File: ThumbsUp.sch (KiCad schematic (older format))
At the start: 153 parts, among them IC1 RP2040, IC2 W25Q128JVSIM, IC3 RP2040, IC4 W25Q128JVSIM, J1 Conn_01x04_Male, J10 Raiser_Male, J11 Raiser_Female, J12 Raiser_Male, J13 Raiser_Female, J14 Raiser_Male, J15 Raiser_Female, J16 Raiser_Male, J17 Raiser_Female, J18 Raiser_Male, J19 Raiser_Female, J2 Conn_01x04_Male, J20 Conn_01x04_Female, J21 Conn_01x04_Female, J22 Conn_01x04_Female, J23 Conn_01x04_Female, J24 Conn_01x04_Male, J25 Conn_01x04_Male, J26 Conn_01x04_Male, J27 Conn_01x04_Male, J28 Conn_01x04_Female, J29 Conn_01x04_Female, J3 Conn_01x04_Female, J30 Conn_01x04_Female, J31 Conn_01x04_Female, J32 USB_C_Receptacle_USB2.0, J33 Raiser_Male, J34 Raiser_Female, J35 Raiser_Male, J36 STX-3501-3N, J37 USB_C_Receptacle_USB2.0, J38 Raiser_Female, J39 Raiser_Male, J4 Conn_01x04_Male, J40 Raiser_Female, J41 Raiser_Male, J42 Raiser_Female, J43 Raiser_Male, J44 Raiser_Female, J45 Raiser_Male, J46 STX-3501-3N, J47 Raiser_Female, J48 Raiser_Male, J5 Conn_01x04_Female, J6 Conn_01x04_Male, J7 Conn_01x04_Male, J8 Conn_01x04_Male, J9 Raiser_Female, U1 NCP1117-3.3_SOT223, U2 NCP1117-3.3_SOT223, Y1 ABLS-12.000MHZ-B4-T, Y2 ABLS-12.000MHZ-B4-T

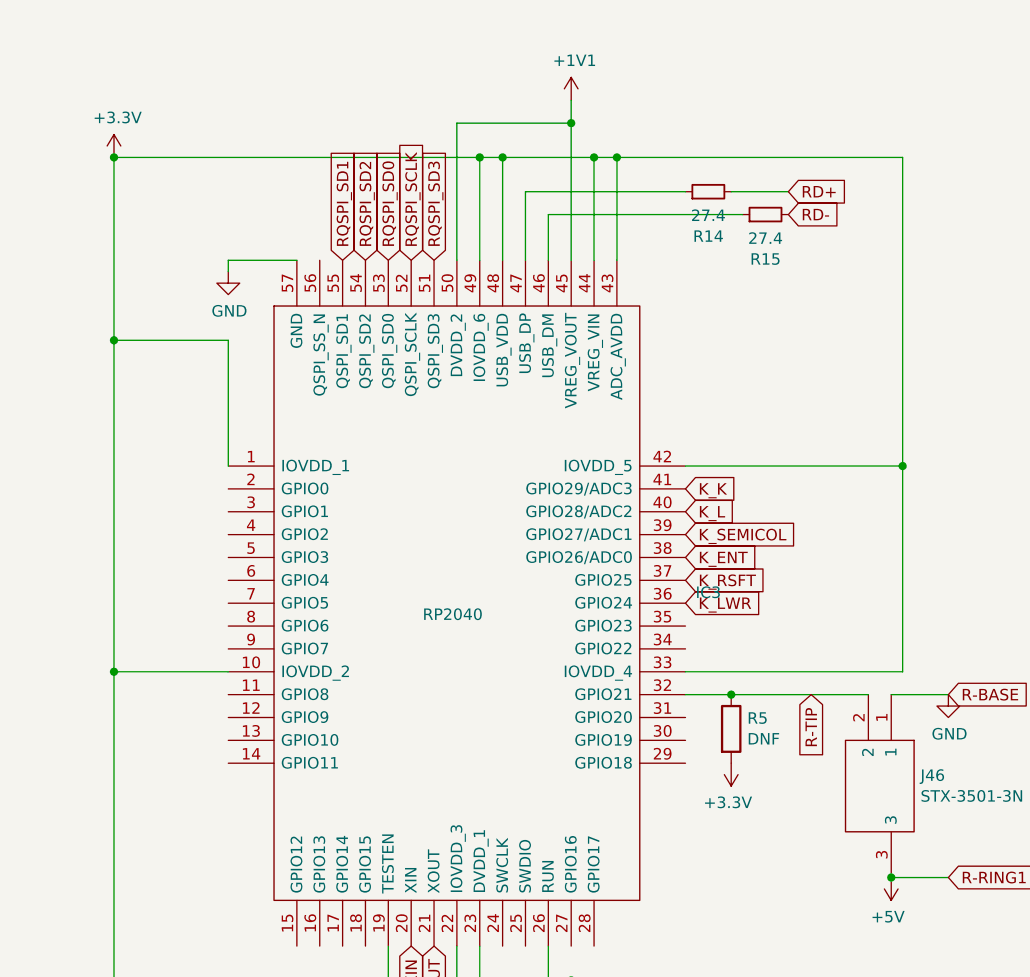
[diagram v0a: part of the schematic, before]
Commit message: Tracing the plates.
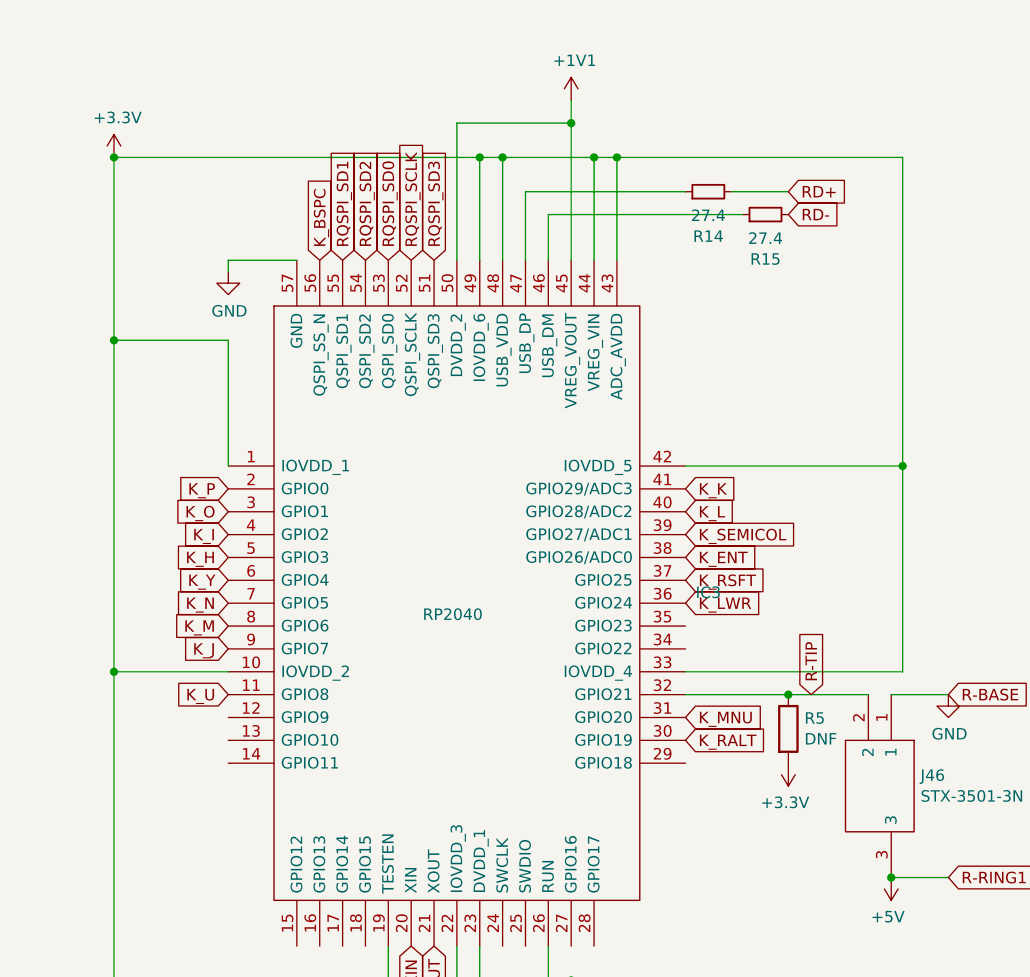
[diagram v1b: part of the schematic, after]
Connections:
- net K_BSPC: now also IC3.56 (QSPI_SS_N)
- net K_H: now also IC3.5 (GPIO3)
- net K_I: now also IC3.4 (GPIO2)
- net K_J: now also IC3.9 (GPIO7)
- net K_M: now also IC3.8 (GPIO6)
- net K_MNU: now also IC3.31 (GPIO20)
- net K_N: now also IC3.7 (GPIO5)
- net K_O: now also IC3.3 (GPIO1)
- net K_P: now also IC3.2 (GPIO0)
- net K_RALT: now also IC3.30 (GPIO19)
- net K_U: now also IC3.11 (GPIO8)
- net K_Y: now also IC3.6 (GPIO4)
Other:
- moved on the sheet: R5
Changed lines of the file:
@@
 $EndComp
 Connection ~ 11950 4600
-Wire Wire Line
-	12050 9600 12050 7950
-$Comp
-L RP2040:RP2040 IC3
-U 1 1 63C3395F
-P 12550 7050
-F 0 "IC3" H 14594 6496 50  0000 L CNN
-F 1 "RP2040" H 13400 6400 50  0000 L CNN
-F 2 "RP2040:QFN40P700X700X90-57N-D" H 14400 7750 50  0001 L CNN
-F 3 "https://datasheets.raspberrypi.org/rp2040/rp2040-datasheet.pdf" H 14400 7650 50  0001 L CNN
-F 4 "Microcontroller in QFN Package" H 14400 7550 50  0001 L CNN "Description"
-F 5 "0.9" H 14400 7450 50  0001 L CNN "Height"
-F 6 "RASPBERRY-PI" H 14400 7350 50  0001 L CNN "Manufacturer_Name"
-F 7 "RP2040" H 14400 7250 50  0001 L CNN "Manufacturer_Part_Number"
-F 8 "" H 14400 7150 50  0001 L CNN "Mouser Part Number"
-F 9 "" H 14400 7050 50  0001 L CNN "Mouser Price/Stock"
-F 10 "" H 14400 6950 50  0001 L CNN "Arrow Part Number"
-F 11 "" H 14400 6850 50  0001 L CNN "Arrow Price/Stock"
-F 12 "" H 14400 6750 50  0001 L CNN "Mouser Testing Part Number"
-F 13 "" H 14400 6650 50  0001 L CNN "Mouser Testing Price/Stock"
-	1    12550 7050
-	1    0    0    -1
-$EndComp
 $Comp
 L Device:R_Small R11
@@
 Connection ~ 12050 6500
 Wire Wire Line
-	12050 6500 12050 7950
-Wire Wire Line
 	1750 5750 1750 6600
 Wire Wire Line
@@
 Wire Wire Line
 	15450 8850 15700 8850
-Text GLabel 15100 8050 3    50   Input ~ 0
+Text GLabel 15100 8050 1    50   Input ~ 0
 R-TIP
 Text GLabel 15700 8050 2    50   Input ~ 0
@@
 L Device:R R5
 U 1 1 63C447F1
-P 14750 8200
-F 0 "R5" H 14820 8246 50  0000 L CNN
-F 1 "DNF" H 14820 8155 50  0000 L CNN
-F 2 "Resistor_SMD:R_0805_2012Metric" V 14680 8200 50  0001 C CNN
-F 3 "~" H 14750 8200 50  0001 C CNN
-	1    14750 8200
+P 15000 8200
+F 0 "R5" H 15070 8246 50  0000 L CNN
+F 1 "DNF" H 15070 8155 50  0000 L CNN
+F 2 "Resistor_SMD:R_0805_2012Metric" V 14930 8200 50  0001 C CNN
+F 3 "~" H 15000 8200 50  0001 C CNN
+	1    15000 8200
 	1    0    0    -1
 $EndComp
@@
 L power:+3.3V #PWR0151
 U 1 1 63C447F7
-P 14750 8350
-F 0 "#PWR0151" H 14750 8200 50  0001 C CNN
-F 1 "+3.3V" H 14765 8523 50  0000 C CNN
-F 2 "" H 14750 8350 50  0001 C CNN
-F 3 "" H 14750 8350 50  0001 C CNN
-	1    14750 8350
-	-1   0    0    1
-$EndComp
-Wire Wire Line
-	14550 8050 14750 8050
-Connection ~ 14750 8050
-Wire Wire Line
-	14750 8050 15350 8050
+P 15000 8350
+F 0 "#PWR0151" H 15000 8200 50  0001 C CNN
+F 1 "+3.3V" H 15015 8523 50  0000 C CNN
+F 2 "" H 15000 8350 50  0001 C CNN
+F 3 "" H 15000 8350 50  0001 C CNN
+	1    15000 8350
+	-1   0    0    1
+$EndComp
 Wire Wire Line
 	18500 2450 18800 2450
@@
 Text GLabel 14550 7650 2    50   Input ~ 0
 K_LWR
+Text GLabel 14550 8150 2    50   Input ~ 0
+K_MNU
+Text GLabel 14550 8250 2    50   Input ~ 0
+K_RALT
+Wire Wire Line
+	12050 9600 12050 7950
+Wire Wire Line
+	12050 6500 12050 7950
+$Comp
+L RP2040:RP2040 IC3
+U 1 1 63C3395F
+P 12550 7050
+F 0 "IC3" H 14594 6496 50  0000 L CNN
+F 1 "RP2040" H 13400 6400 50  0000 L CNN
+F 2 "RP2040:QFN40P700X700X90-57N-D" H 14400 7750 50  0001 L CNN
+F 3 "https://datasheets.raspberrypi.org/rp2040/rp2040-datasheet.pdf" H 14400 7650 50  0001 L CNN
+F 4 "Microcontroller in QFN Package" H 14400 7550 50  0001 L CNN "Description"
+F 5 "0.9" H 14400 7450 50  0001 L CNN "Height"
+F 6 "RASPBERRY-PI" H 14400 7350 50  0001 L CNN "Manufacturer_Name"
+F 7 "RP2040" H 14400 7250 50  0001 L CNN "Manufacturer_Part_Number"
+F 8 "" H 14400 7150 50  0001 L CNN "Mouser Part Number"
+F 9 "" H 14400 7050 50  0001 L CNN "Mouser Price/Stock"
+F 10 "" H 14400 6950 50  0001 L CNN "Arrow Part Number"
+F 11 "" H 14400 6850 50  0001 L CNN "Arrow Price/Stock"
+F 12 "" H 14400 6750 50  0001 L CNN "Mouser Testing Part Number"
+F 13 "" H 14400 6650 50  0001 L CNN "Mouser Testing Price/Stock"
+	1    12550 7050
+	1    0    0    -1
+$EndComp
+Connection ~ 15000 8050
+Wire Wire Line
+	15000 8050 15350 8050
+Wire Wire Line
+	14550 8050 15000 8050
+Text GLabel 12950 6150 1    50   Input ~ 0
+K_BSPC
+Text GLabel 12550 7150 0    50   Input ~ 0
+K_P
+Text GLabel 12550 7250 0    50   Input ~ 0
+K_O
+Text GLabel 12550 7350 0    50   Input ~ 0
+K_I
+Text GLabel 12550 7450 0    50   Input ~ 0
+K_H
+Text GLabel 12550 7550 0    50   Input ~ 0
+K_Y
+Text GLabel 12550 7650 0    50   Input ~ 0
+K_N
+Text GLabel 12550 7750 0    50   Input ~ 0
+K_M
+Text GLabel 12550 7850 0    50   Input ~ 0
+K_J
+Text GLabel 12550 8050 0    50   Input ~ 0
+K_U
 $EndSCHEMATC

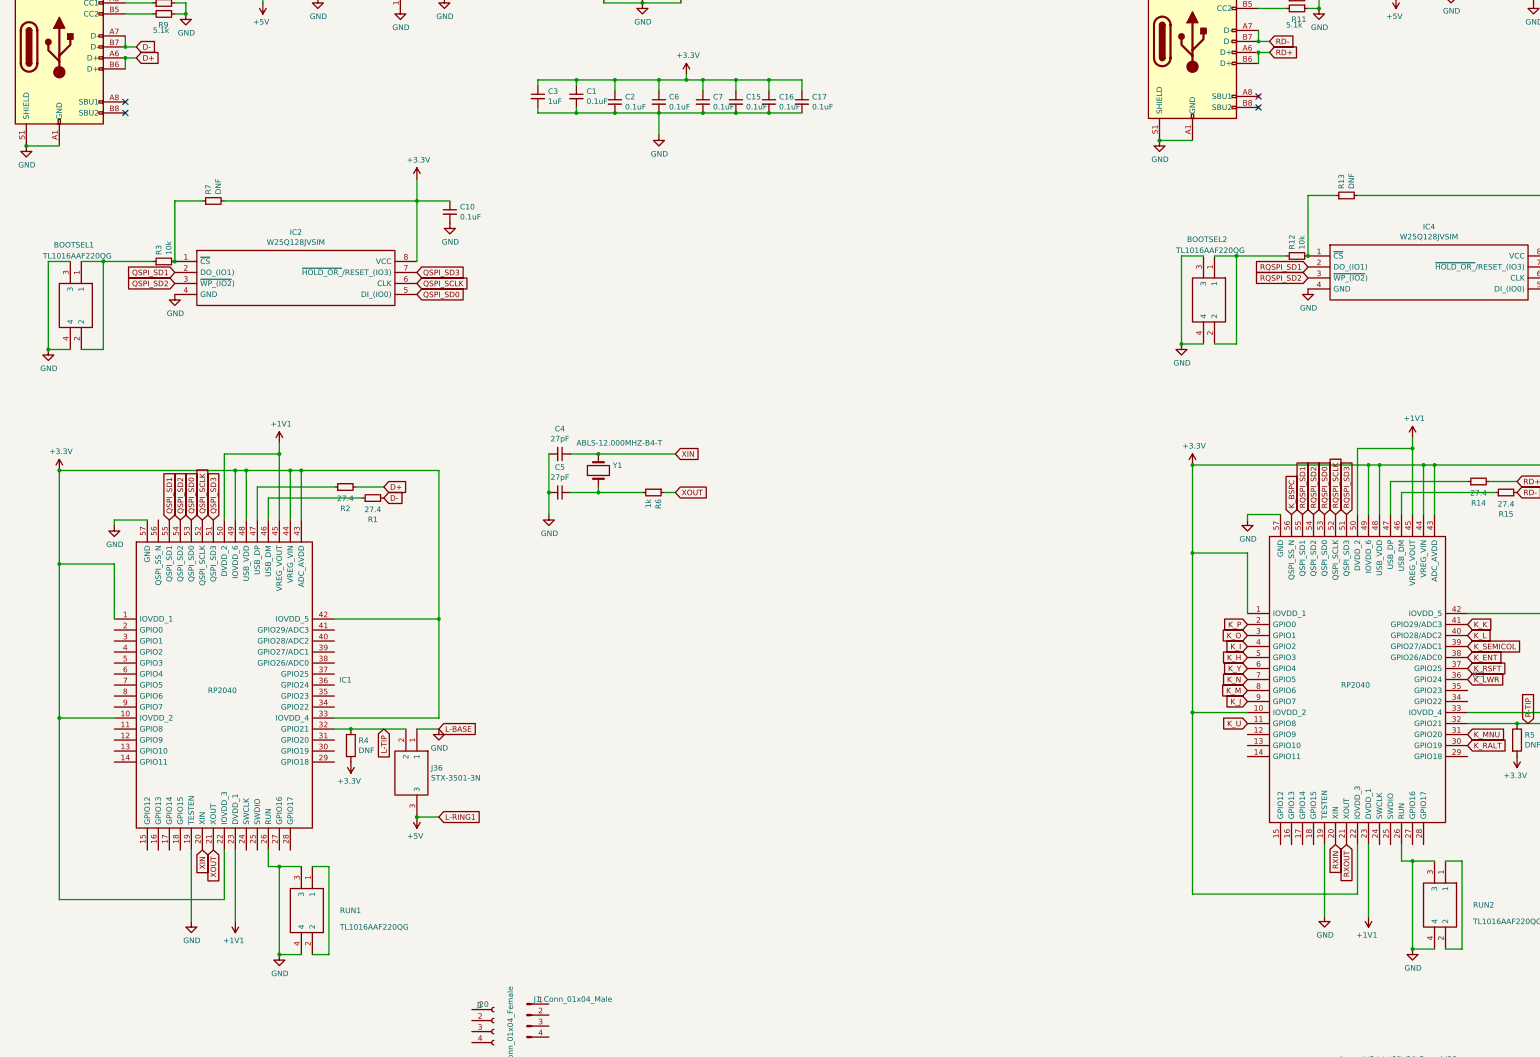
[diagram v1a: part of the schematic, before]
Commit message: Somewhat finished the PCB tracing
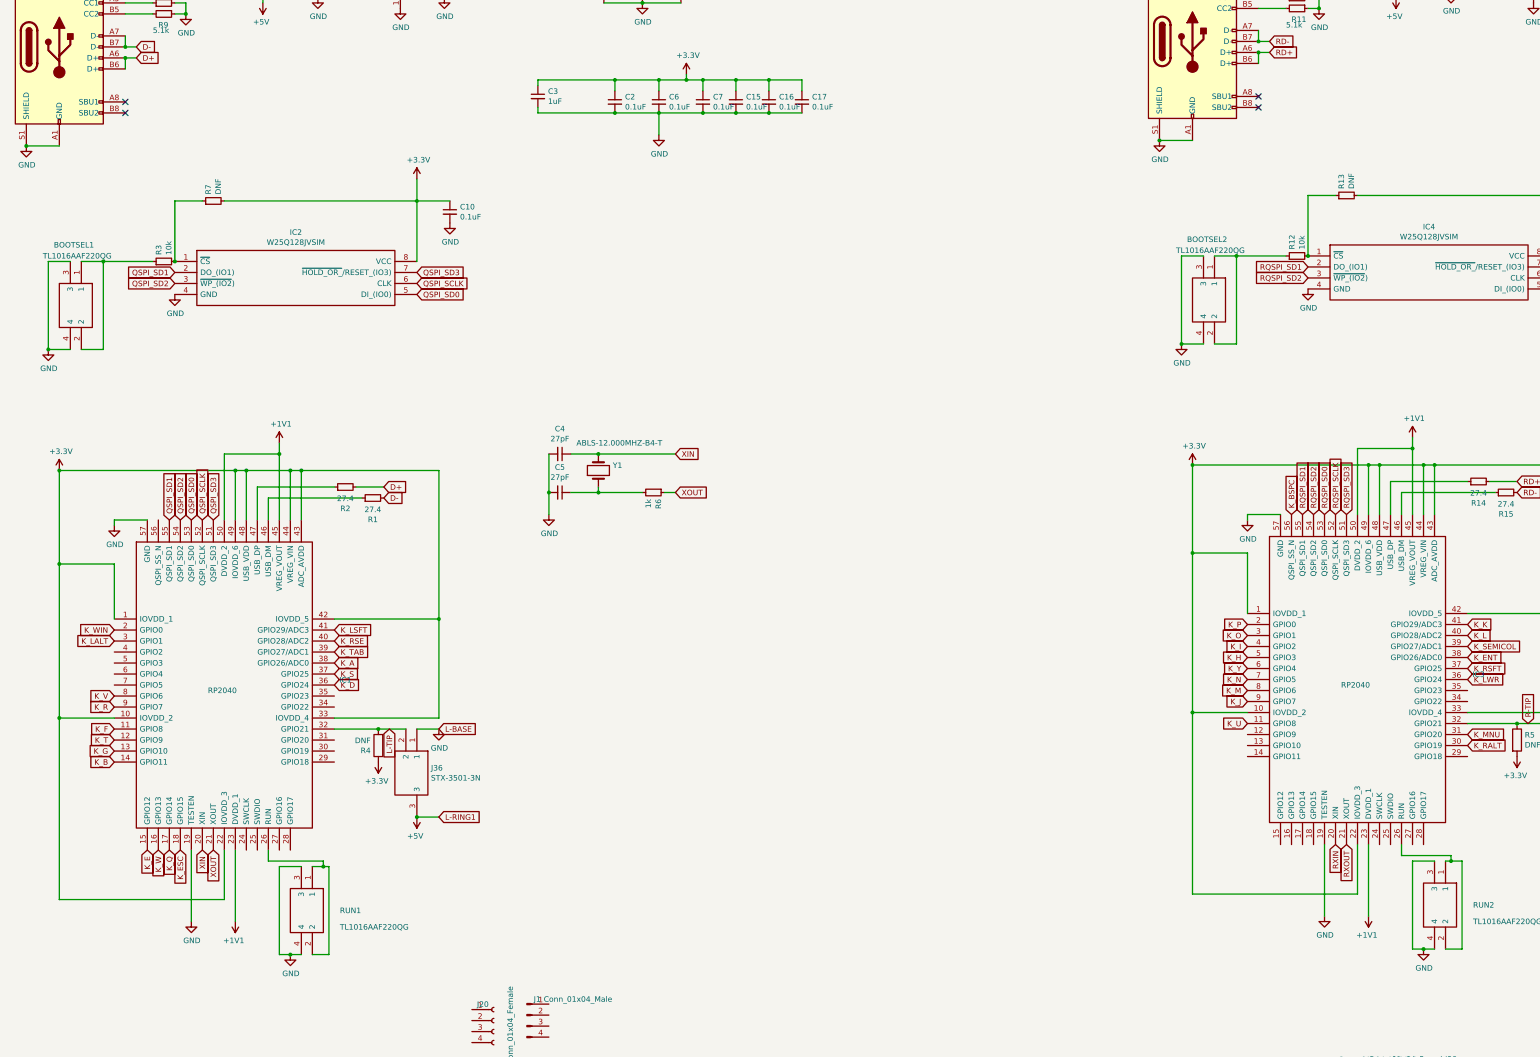
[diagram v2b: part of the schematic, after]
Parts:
- removed C1: 0.1uF, Capacitor_SMD:C_0402_1005Metric, symbol Device:C_Small
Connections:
- net +3V3: now also R4.1; no longer R4.2
- net GND: no longer IC1.26 (RUN), IC3.26 (RUN)
- net K_A: now also IC1.38 (GPIO26/ADC0)
- net K_B: now also IC1.14 (GPIO11)
- net K_D: now also IC1.36 (GPIO24)
- net K_E: now also IC1.15 (GPIO12)
- net K_ESC: now also IC1.18 (GPIO15)
- net K_F: now also IC1.11 (GPIO8)
- net K_G: now also IC1.13 (GPIO10)
- net K_LALT: now also IC1.3 (GPIO1)
- net K_LSFT: now also IC1.41 (GPIO29/ADC3)
- net K_Q: now also IC1.17 (GPIO14)
- net K_R: now also IC1.9 (GPIO7)
- net K_RSE: now also IC1.40 (GPIO28/ADC2)
- net K_S: now also IC1.37 (GPIO25)
- net K_T: now also IC1.12 (GPIO9)
- net K_TAB: now also IC1.39 (GPIO27/ADC1)
- net K_V: now also IC1.8 (GPIO6)
- net K_W: now also IC1.16 (GPIO13)
- net K_WIN: now also IC1.2 (GPIO0)
- net L-TIP: now also R4.2; no longer R4.1
- net at RUN1.1, RUN1.2: now also IC1.26 (RUN)
- net at RUN2.1, RUN2.2: now also IC3.26 (RUN)
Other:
- moved on the sheet: R4
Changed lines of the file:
@@
 Wire Wire Line
 	3300 1300 3600 1300
-$Comp
-L Device:C_Small C1
-U 1 1 6197A27B
-P 6450 2350
-F 0 "C1" H 6542 2396 50  0000 L CNN
-F 1 "0.1uF" H 6542 2305 50  0000 L CNN
-F 2 "Capacitor_SMD:C_0402_1005Metric" H 6450 2350 50  0001 C CNN
-F 3 "~" H 6450 2350 50  0001 C CNN
-	1    6450 2350
-	1    0    0    -1
-$EndComp
-Wire Wire Line
-	6800 2500 6450 2500
-Wire Wire Line
-	6450 2500 6450 2450
 Connection ~ 6800 2500
-Wire Wire Line
-	6800 2200 6450 2200
-Wire Wire Line
-	6450 2200 6450 2250
 Connection ~ 6800 2200
 Wire Wire Line
@@
 	6100 2250 6100 2200
 Wire Wire Line
-	6100 2200 6450 2200
-Connection ~ 6450 2200
-Wire Wire Line
 	6100 2450 6100 2500
-Wire Wire Line
-	6100 2500 6450 2500
-Connection ~ 6450 2500
 $Comp
 L Device:C_Small C13
@@
 L power:GND #PWR0117
 U 1 1 63E16CE5
-P 3750 10150
-F 0 "#PWR0117" H 3750 9900 50  0001 C CNN
-F 1 "GND" H 3755 9977 50  0000 C CNN
-F 2 "" H 3750 10150 50  0001 C CNN
-F 3 "" H 3750 10150 50  0001 C CNN
-	1    3750 10150
+P 3850 10150
+F 0 "#PWR0117" H 3850 9900 50  0001 C CNN
+F 1 "GND" H 3855 9977 50  0000 C CNN
+F 2 "" H 3850 10150 50  0001 C CNN
+F 3 "" H 3850 10150 50  0001 C CNN
+	1    3850 10150
 	1    0    0    -1
 $EndComp
@@
 $EndComp
 Wire Wire Line
-	4050 9350 4200 9350
+	4050 9350 4150 9350
 Wire Wire Line
 	4200 9350 4200 10150
 Wire Wire Line
-	4200 10150 4050 10150
-Wire Wire Line
-	3750 10150 3950 10150
+	3750 10150 3850 10150
 $Comp
 L TL1016AAF220QG:TL1016AAF220QG BOOTSEL1
@@
 Connection ~ 2350 2000
 Wire Wire Line
-	3650 9350 3650 9200
-Wire Wire Line
-	3650 9350 3750 9350
-Wire Wire Line
 	3750 10150 3750 9350
-Connection ~ 3750 10150
-Connection ~ 3750 9350
 Wire Wire Line
 	3750 9350 3950 9350
@@
 L power:GND #PWR0143
 U 1 1 63C338F1
-P 14050 10100
-F 0 "#PWR0143" H 14050 9850 50  0001 C CNN
-F 1 "GND" H 14055 9927 50  0000 C CNN
-F 2 "" H 14050 10100 50  0001 C CNN
-F 3 "" H 14050 10100 50  0001 C CNN
-	1    14050 10100
+P 14150 10100
+F 0 "#PWR0143" H 14150 9850 50  0001 C CNN
+F 1 "GND" H 14155 9927 50  0000 C CNN
+F 2 "" H 14150 10100 50  0001 C CNN
+F 3 "" H 14150 10100 50  0001 C CNN
+	1    14150 10100
 	1    0    0    -1
 $EndComp
@@
 $EndComp
 Wire Wire Line
-	14350 9300 14500 9300
+	14350 9300 14400 9300
 Wire Wire Line
 	14500 9300 14500 10100
-Wire Wire Line
-	14500 10100 14350 10100
-Wire Wire Line
-	14050 10100 14250 10100
 $Comp
 L TL1016AAF220QG:TL1016AAF220QG BOOTSEL2
@@
 	12650 1950 12750 1950
 Connection ~ 12650 1950
-Wire Wire Line
-	13950 9300 13950 9150
-Wire Wire Line
-	13950 9300 14050 9300
-Wire Wire Line
-	14050 10100 14050 9300
-Connection ~ 14050 10100
-Connection ~ 14050 9300
-Wire Wire Line
-	14050 9300 14250 9300
 Text GLabel 13100 3900 0    50   Input ~ 0
 RQSPI_SD1
@@
 Wire Wire Line
 	5000 8900 5200 8900
-Text GLabel 4700 8100 3    50   Input ~ 0
+Text GLabel 4750 8100 3    50   Input ~ 0
 L-TIP
 Text GLabel 5200 8100 2    50   Input ~ 0
@@
 $EndComp
 Connection ~ 15450 8850
-Wire Wire Line
-	4250 8100 4400 8100
 $Comp
 L Device:R R4
 U 1 1 63C3C97D
-P 4400 8250
-F 0 "R4" H 4470 8296 50  0000 L CNN
-F 1 "DNF" H 4470 8205 50  0000 L CNN
-F 2 "Resistor_SMD:R_0805_2012Metric" V 4330 8250 50  0001 C CNN
-F 3 "~" H 4400 8250 50  0001 C CNN
-	1    4400 8250
-	1    0    0    -1
+P 4650 8250
+F 0 "R4" H 4720 8296 50  0000 L CNN
+F 1 "DNF" H 4720 8205 50  0000 L CNN
+F 2 "Resistor_SMD:R_0805_2012Metric" V 4580 8250 50  0001 C CNN
+F 3 "~" H 4650 8250 50  0001 C CNN
+	1    4650 8250
+	-1   0    0    1
 $EndComp
-Connection ~ 4400 8100
-Wire Wire Line
-	4400 8100 4900 8100
 $Comp
 L power:+3.3V #PWR0150
 U 1 1 63C3E3CC
-P 4400 8400
-F 0 "#PWR0150" H 4400 8250 50  0001 C CNN
-F 1 "+3.3V" H 4415 8573 50  0000 C CNN
-F 2 "" H 4400 8400 50  0001 C CNN
-F 3 "" H 4400 8400 50  0001 C CNN
-	1    4400 8400
+P 4650 8400
+F 0 "#PWR0150" H 4650 8250 50  0001 C CNN
+F 1 "+3.3V" H 4665 8573 50  0000 C CNN
+F 2 "" H 4650 8400 50  0001 C CNN
+F 3 "" H 4650 8400 50  0001 C CNN
+	1    4650 8400
 	-1   0    0    1
 $EndComp
@@
 Text GLabel 12550 8050 0    50   Input ~ 0
 K_U
+Wire Wire Line
+	14050 10100 14150 10100
+Wire Wire Line
+	14050 9300 14250 9300
+Wire Wire Line
+	14050 10100 14050 9300
+Wire Wire Line
+	3650 9200 3650 9300
+Wire Wire Line
+	3650 9300 4150 9300
+Wire Wire Line
+	4150 9300 4150 9350
+Connection ~ 4150 9350
+Wire Wire Line
+	4150 9350 4200 9350
+Connection ~ 3850 10150
+Wire Wire Line
+	3850 10150 3950 10150
+Wire Wire Line
+	4050 10150 4200 10150
+Wire Wire Line
+	13950 9150 13950 9250
+Wire Wire Line
+	13950 9250 14400 9250
+Wire Wire Line
+	14400 9250 14400 9300
+Connection ~ 14400 9300
+Wire Wire Line
+	14400 9300 14500 9300
+Connection ~ 14150 10100
+Wire Wire Line
+	14150 10100 14250 10100
+Wire Wire Line
+	14350 10100 14500 10100
+Text GLabel 4250 7200 2    50   Input ~ 0
+K_LSFT
+Text GLabel 4250 7300 2    50   Input ~ 0
+K_RSE
+Text GLabel 4250 7400 2    50   Input ~ 0
+K_TAB
+Text GLabel 4250 7500 2    50   Input ~ 0
+K_A
+Text GLabel 4250 7600 2    50   Input ~ 0
+K_S
+Text GLabel 4250 7700 2    50   Input ~ 0
+K_D
+Text GLabel 2850 9200 3    50   Input ~ 0
+K_ESC
+Text GLabel 2750 9200 3    50   Input ~ 0
+K_Q
+Wire Wire Line
+	4250 8100 4650 8100
+Connection ~ 4650 8100
+Wire Wire Line
+	4650 8100 4900 8100
+Text GLabel 2650 9200 3    50   Input ~ 0
+K_W
+Text GLabel 2550 9200 3    50   Input ~ 0
+K_E
+Text GLabel 2250 8400 0    50   Input ~ 0
+K_B
+Text GLabel 2250 8300 0    50   Input ~ 0
+K_G
+Text GLabel 2250 8200 0    50   Input ~ 0
+K_T
+Text GLabel 2250 8100 0    50   Input ~ 0
+K_F
+Text GLabel 2250 7900 0    50   Input ~ 0
+K_R
+Text GLabel 2250 7800 0    50   Input ~ 0
+K_V
+Wire Wire Line
+	6100 2200 6800 2200
+Wire Wire Line
+	6100 2500 6800 2500
+Text GLabel 2250 7200 0    50   Input ~ 0
+K_WIN
+Text GLabel 2250 7300 0    50   Input ~ 0
+K_LALT
 $EndSCHEMATC
